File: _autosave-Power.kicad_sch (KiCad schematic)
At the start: 30 parts

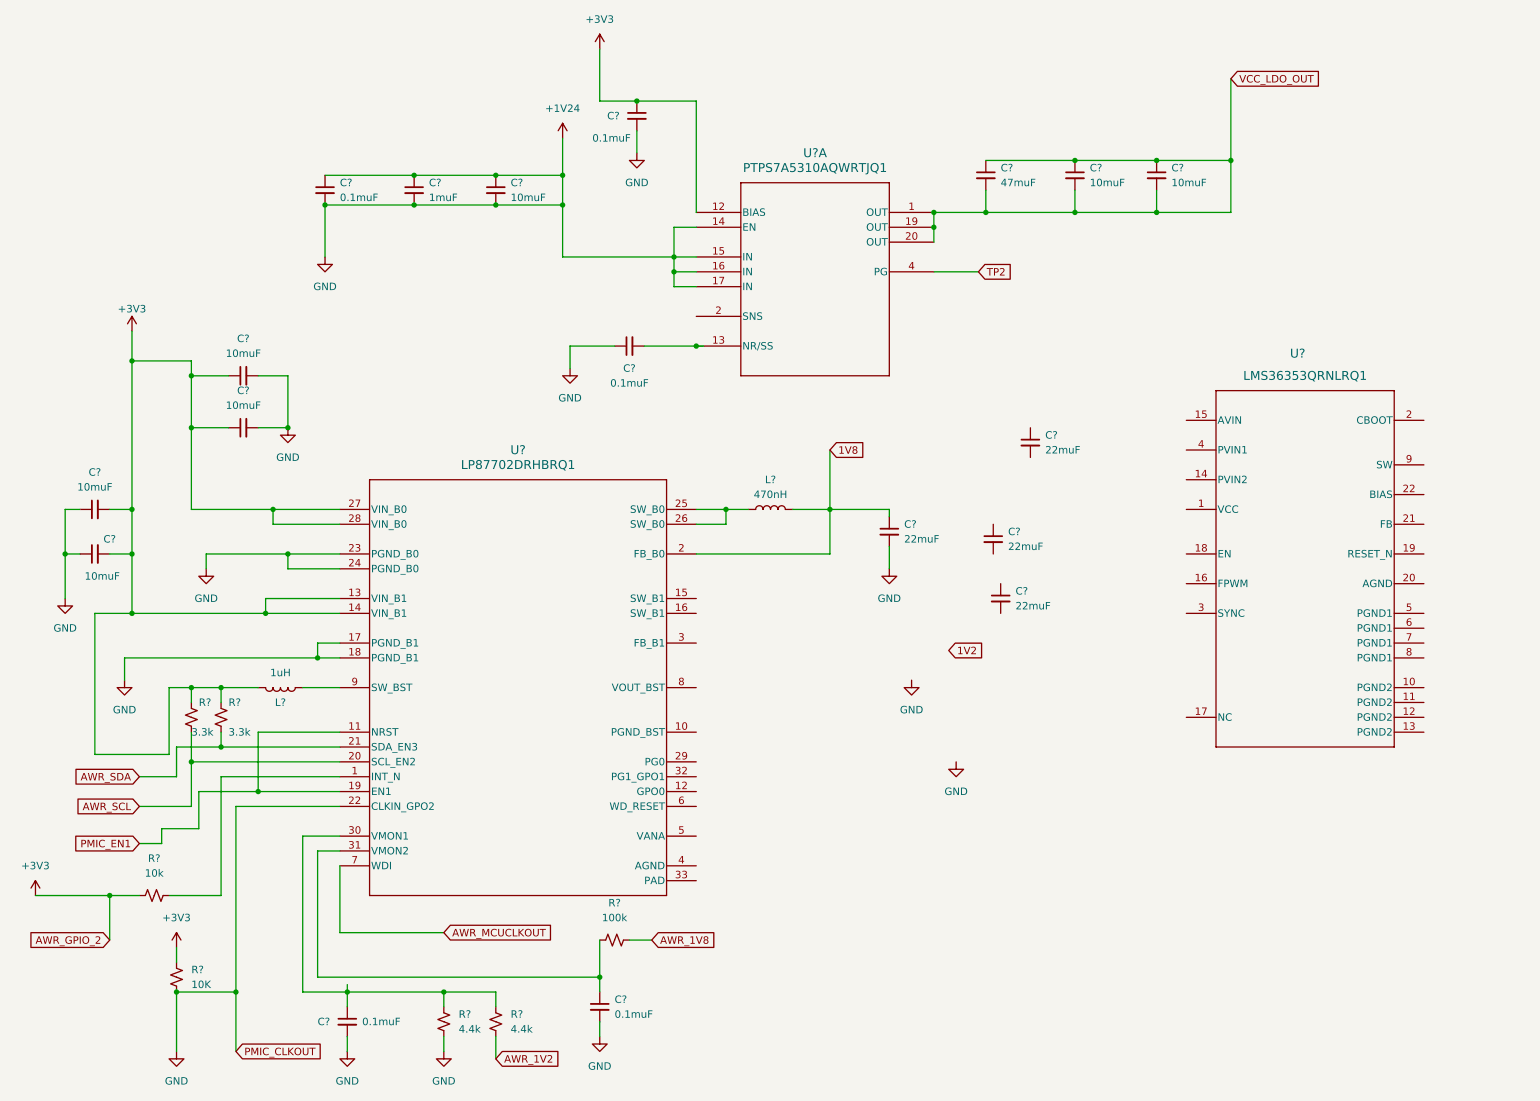
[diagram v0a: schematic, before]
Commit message: finished buck converter, new sheet for ldo and step down
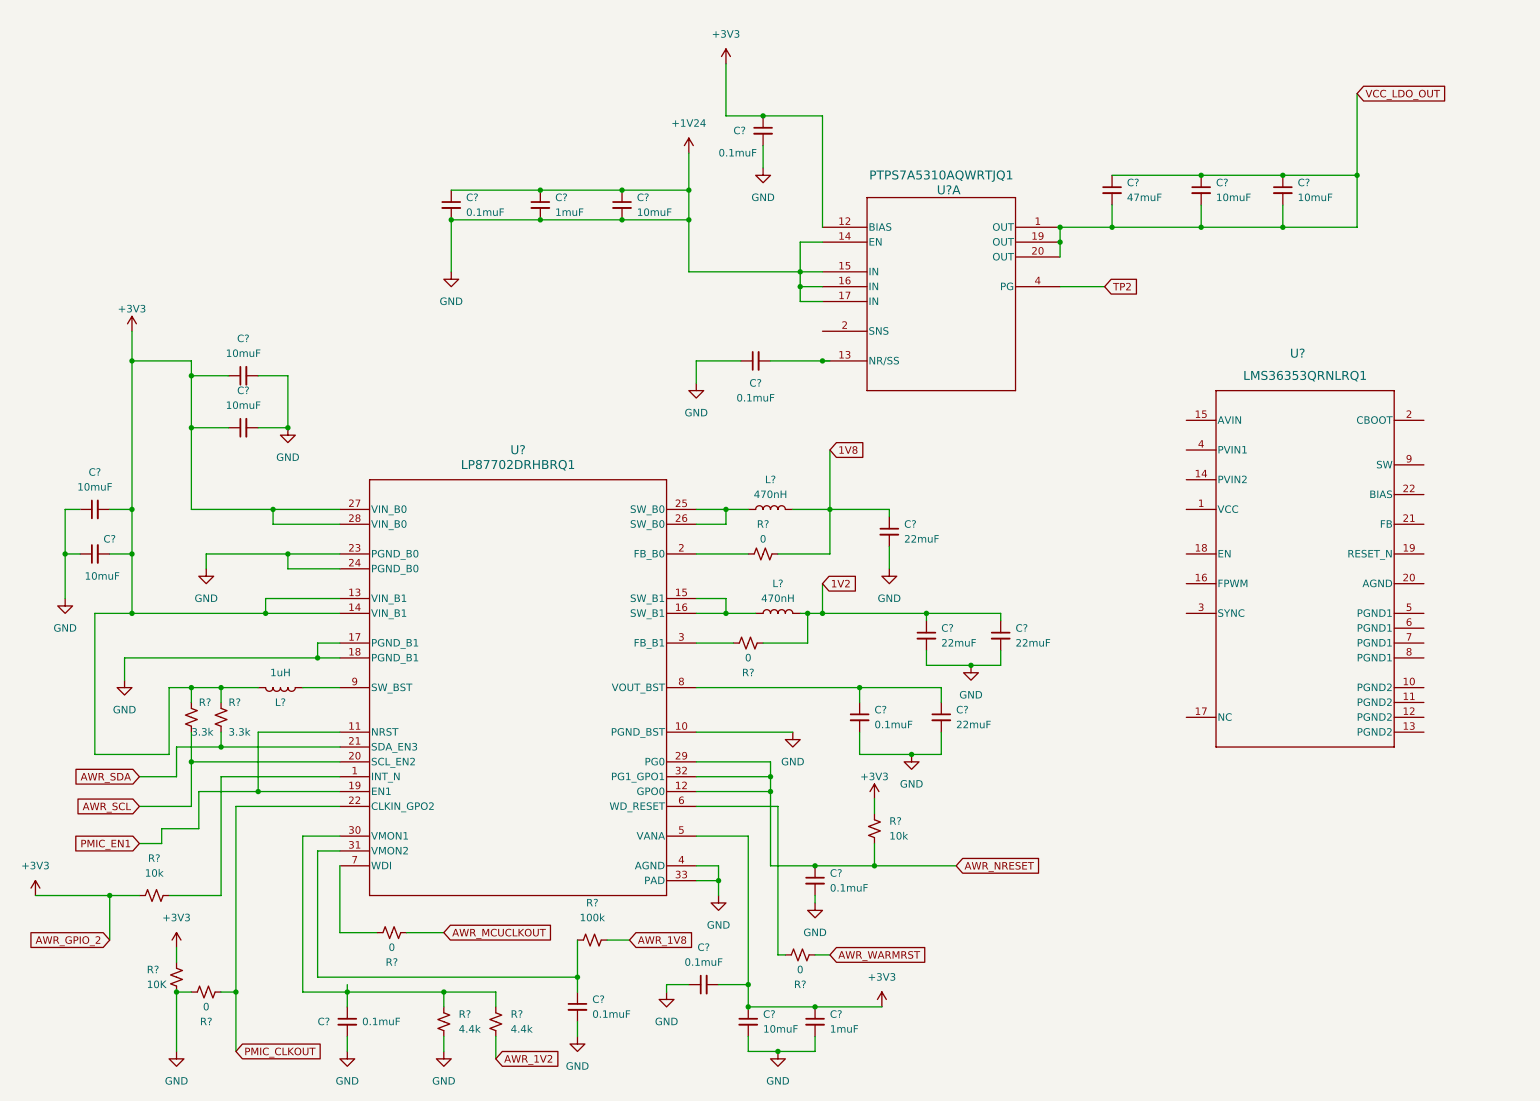
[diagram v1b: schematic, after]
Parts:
- added C? (x3): 0.1muF, symbol Device:C_Small
- added C?: 10muF, symbol Device:C_Small
- added C?: 1muF, symbol Device:C_Small
- added L?: 470nH, symbol Device:L
- added R? (x5): 0, symbol Device:R_Small_US
- added R?: 10k, symbol Device:R_Small_US
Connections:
- net +1V35: now also C?.2, C?.2, C?.2, U?.10 (PGND_BST), U?.33 (PAD), U?.4 (AGND), C?.1, C?.2, C?.2, C?.2, C?.2, R?.2; no longer U?.22 (CLKIN_GPO2)
- net +3V3: now also U?.5 (VANA), C?.1, C?.1, C?.2, R?.1
- net 1V2: now also C?.1, C?.1, L?.2, R?.1
- net 1V8: now also R?.2; no longer U?.2 (FB_B0)
- net AWR_MCUCLKOUT: now also R?.1; no longer U?.7 (WDI)
- net AWR_NRESET: now reaches U?.12 (GPO0)
- net AWR_NRESET: now also U?.29 (PG0), U?.32 (PG1_GPO1), C?.1, R?.2
- net at U?.15 (SW_B1): now also U?.16 (SW_B1), L?.1
- net at U?.3 (FB_B1): now also R?.2
- net at U?.6 (WD_RESET): now also R?.2
- net at U?.8 (VOUT_BST): now also C?.1, C?.1
- new net: R?.1, U?.2 (FB_B0)
- new net: R?.2, U?.7 (WDI)
- new net AWR_WARMRST: R?.1
- new net PMIC_CLKOUT: R?.1, U?.22 (CLKIN_GPO2)
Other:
- moved on the sheet: C?, R?, U?A

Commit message: adding our charge controller and usbc connector
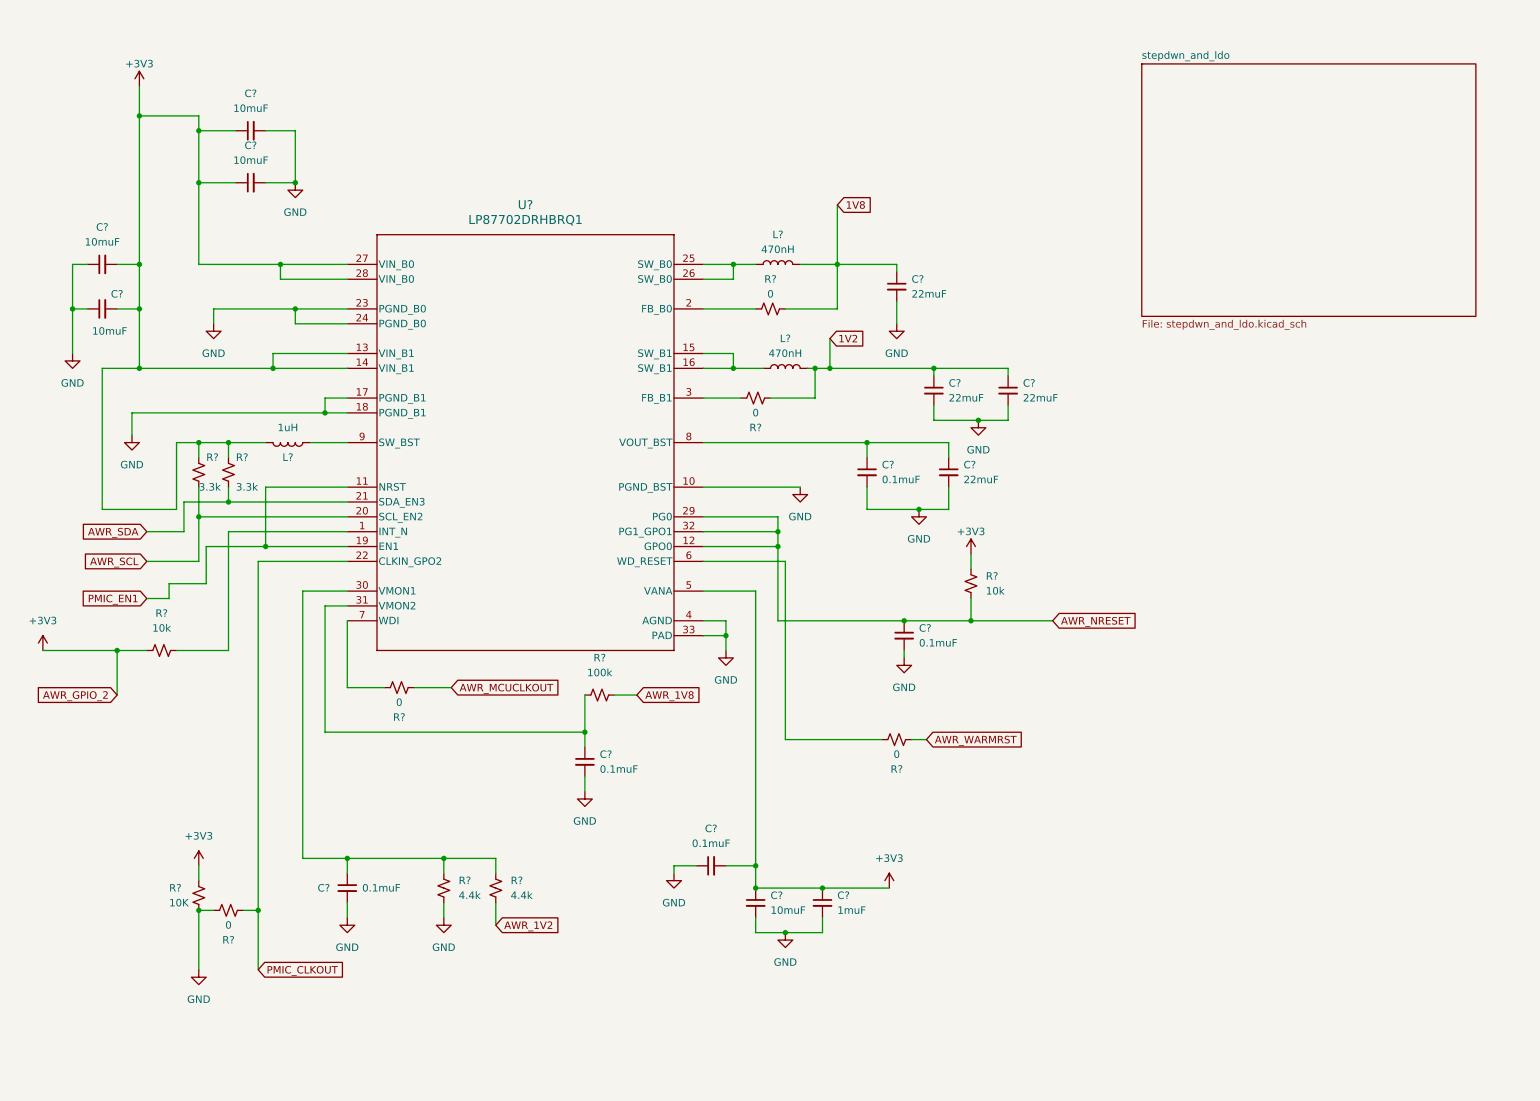
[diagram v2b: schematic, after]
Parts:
- removed C? (x3): 10muF, symbol Device:C_Small
- removed C? (x3): 0.1muF, symbol Device:C_Small
- removed C?: 1muF, symbol Device:C_Small
- removed C?: 47muF, symbol Device:C_Small
- removed U?: LMS36353QRNLRQ1, RNL0022A, symbol LMS3635-Q1:LMS36353QRNLRQ1
- removed U?: PTPS7A5310AQWRTJQ1, WQFN20_RTJ_TEX, symbol TPS7A5301QRGRRQ1:PTPS7A5310AQWRTJQ1
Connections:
- net +1V35 renamed GND
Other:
- added sheet stepdwn_and_ldo (stepdwn_and_ldo.kicad_sch)
- moved on the sheet: C?, L?, R?, U?

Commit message: squasing ERC errors
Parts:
- added R26, R27: 0, symbol Device:R_Small_US
- gave numbers to parts that had none: 32
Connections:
- net AWR_NRESET: now also R26.2, R27.2; no longer U1.12 (GPO0), U1.29 (PG0), U1.32 (PG1_GPO1)
- new net: R27.1, U1.12 (GPO0)
- new net: R26.1, U1.29 (PG0)
- no-connect marks 0 -> 1
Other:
- moved on the sheet: C30

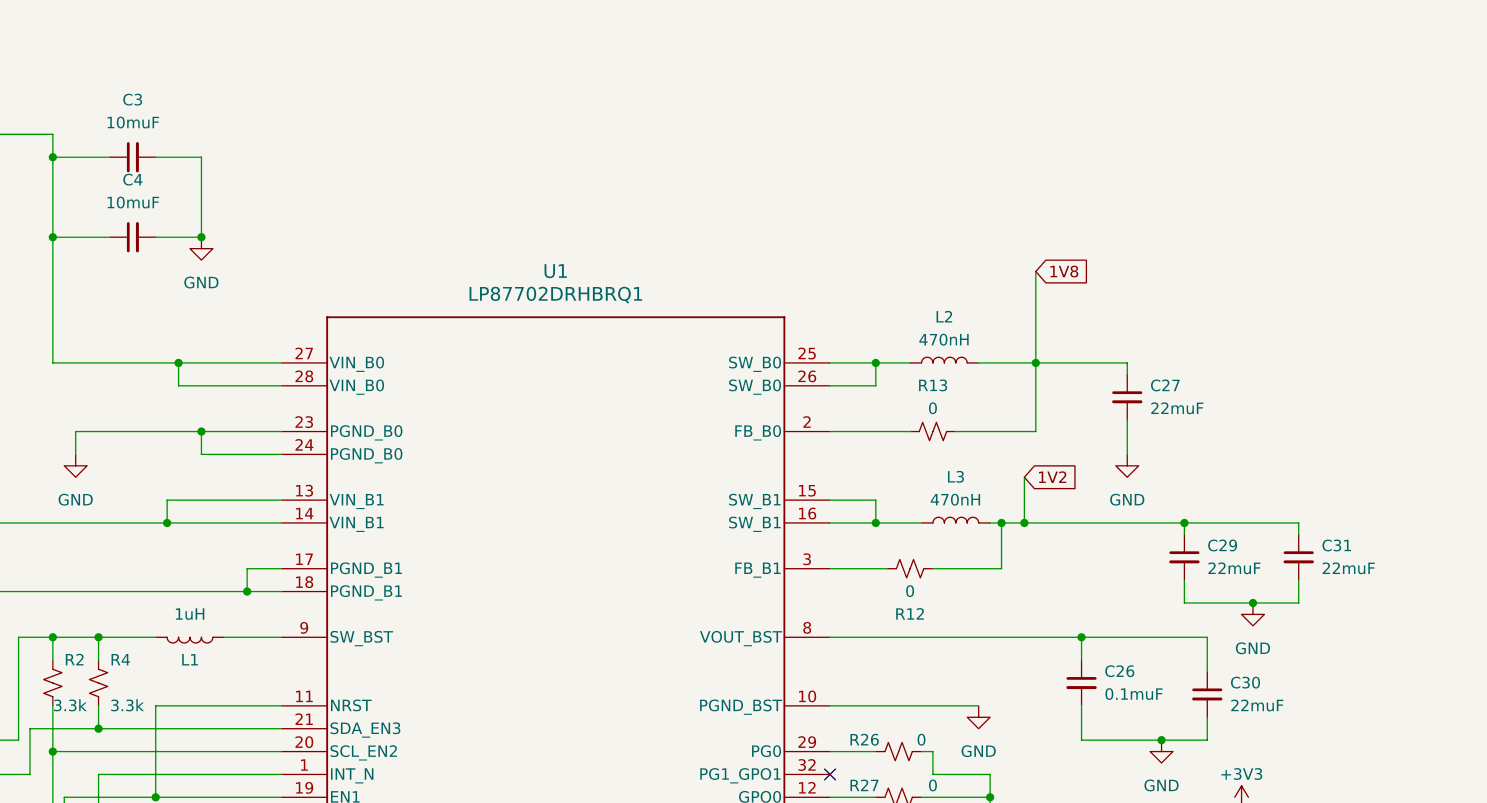
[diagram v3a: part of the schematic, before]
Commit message: making unit design for AWR1843, starting with GND, voltage, I2C and GPIO
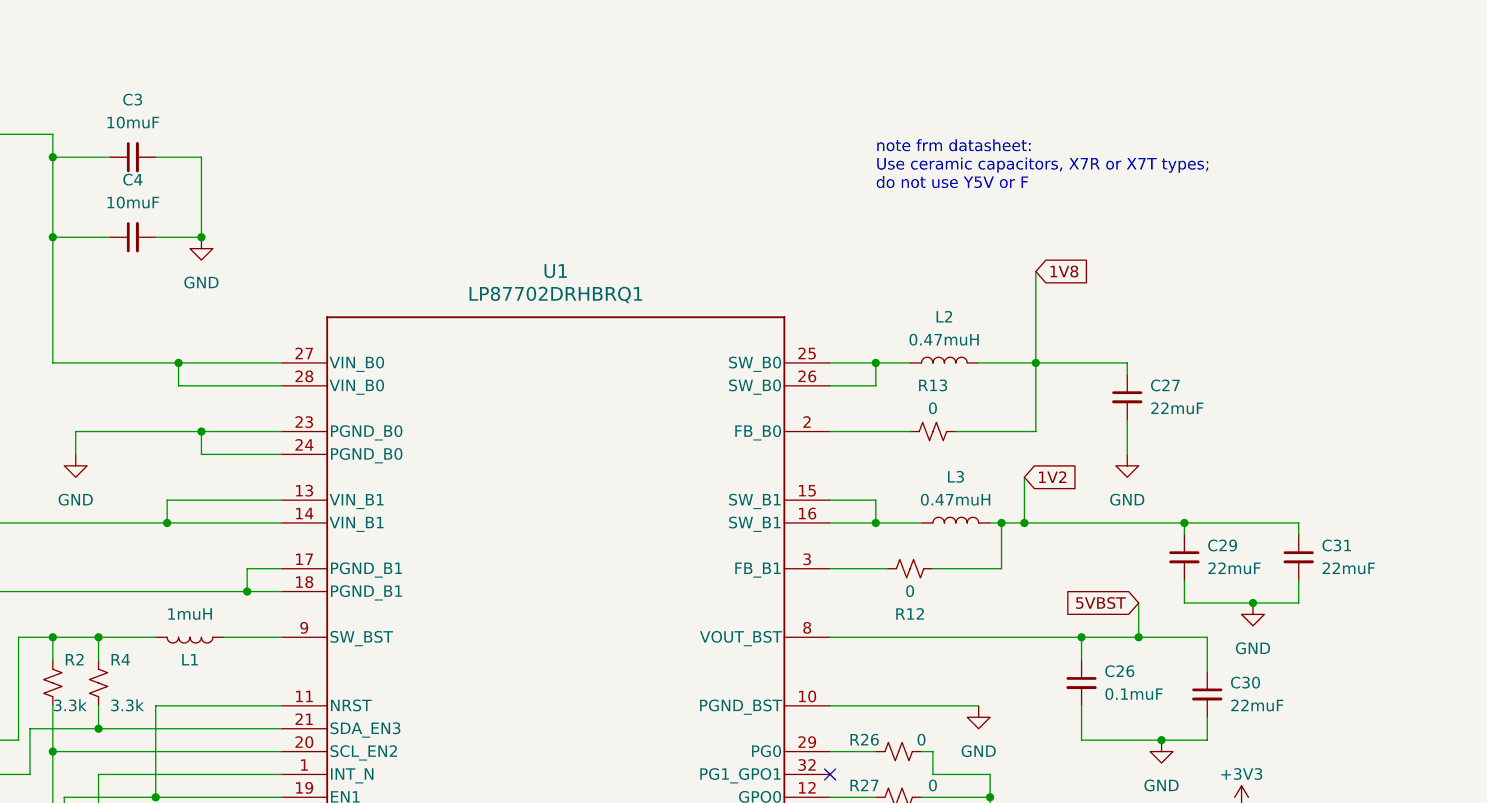
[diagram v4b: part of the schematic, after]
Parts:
- L1: value 1uH -> 1muH
- L2, L3: value 470nH -> 0.47muH
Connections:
- net 5VBST: now reaches C26.1, C30.1, U1.8 (VOUT_BST)
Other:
- note added: "note frm datasheet: Use ceramic capacitors, X7R or X7T types; do not use Y5V or F"
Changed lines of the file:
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@@
   (junction (at 140.97 119.38) (diameter 0) (color 0 0 0 0)
+  )
+  (junction (at 171.45 86.36) (diameter 0) (color 0 0 0 0)
   )
   (junction (at 182.88 116.84) (diameter 0) (color 0 0 0 0)
@@
     (stroke (width 0) (type default))
   )
-  (wire (pts (xy 165.1 86.36) (xy 179.07 86.36))
+  (wire (pts (xy 165.1 86.36) (xy 171.45 86.36))
     (stroke (width 0) (type default))
   )
@@
     (stroke (width 0) (type default))
   )
+  (wire (pts (xy 171.45 82.55) (xy 171.45 86.36))
+    (stroke (width 0) (type default))
+  )
   (wire (pts (xy 36.83 121.92) (xy 36.83 129.54))
     (stroke (width 0) (type default))
@@
     (stroke (width 0) (type default))
   )
+  (wire (pts (xy 171.45 86.36) (xy 179.07 86.36))
+    (stroke (width 0) (type default))
+  )
   (wire (pts (xy 135.89 158.75) (xy 132.08 158.75))
     (stroke (width 0) (type default))
@@
   (wire (pts (xy 92.71 165.1) (xy 92.71 167.64))
     (stroke (width 0) (type default))
+  )
+  (text "note frm datasheet:\nUse ceramic capacitors, X7R or X7T types; \ndo not use Y5V or F"
+    (at 142.24 36.83 0)
+    (effects (font (size 1.27 1.27)) (justify left bottom))
   )
   (global_label "PMIC_EN1" (shape input) (at 41.91 113.03 180) (fields_autoplaced)
@@
     (property "Intersheetrefs" "${INTERSHEET_REFS}" (at 112.9914 128.27 0)
       (effects (font (size 1.27 1.27)) (justify left) hide)
+    )
+  )
+  (global_label "5VBST" (shape input) (at 171.45 82.55 180) (fields_autoplaced)
+    (effects (font (size 1.27 1.27)) (justify right))
+    (property "Intersheetrefs" "${INTERSHEET_REFS}" (at 162.7196 82.55 0)
+      (effects (font (size 1.27 1.27)) (justify right) hide)
     )
   )
@@
       (effects (font (size 1.27 1.27)))
     )
-    (property "Value" "470nH" (at 151.13 71.12 90)
+    (property "Value" "0.47muH" (at 151.13 71.12 90)
       (effects (font (size 1.27 1.27)))
     )
@@
       (effects (font (size 1.27 1.27)))
     )
-    (property "Value" "1uH" (at 66.04 83.82 90)
+    (property "Value" "1muH" (at 66.04 83.82 90)
       (effects (font (size 1.27 1.27)))
     )
@@
       (effects (font (size 1.27 1.27)))
     )
-    (property "Value" "470nH" (at 149.86 53.34 90)
-      (effects (font (size 1.27 1.27)))
-    )
+    (property "Value" "0.47muH" (at 149.86 53.34 90)
+      (effects (font (size 1.27 1.27)))
+    )
